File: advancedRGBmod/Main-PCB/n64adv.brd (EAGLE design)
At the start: 64.5 x 37.7 mm, 112 parts, among them U1 10CL010YE144, U2 ADV7125/ADV7123, U4 74LVC3G17, U5 S25FLXXXSO8-DUAL, U6 TLV70012DDC, U7 TLV70025DDC

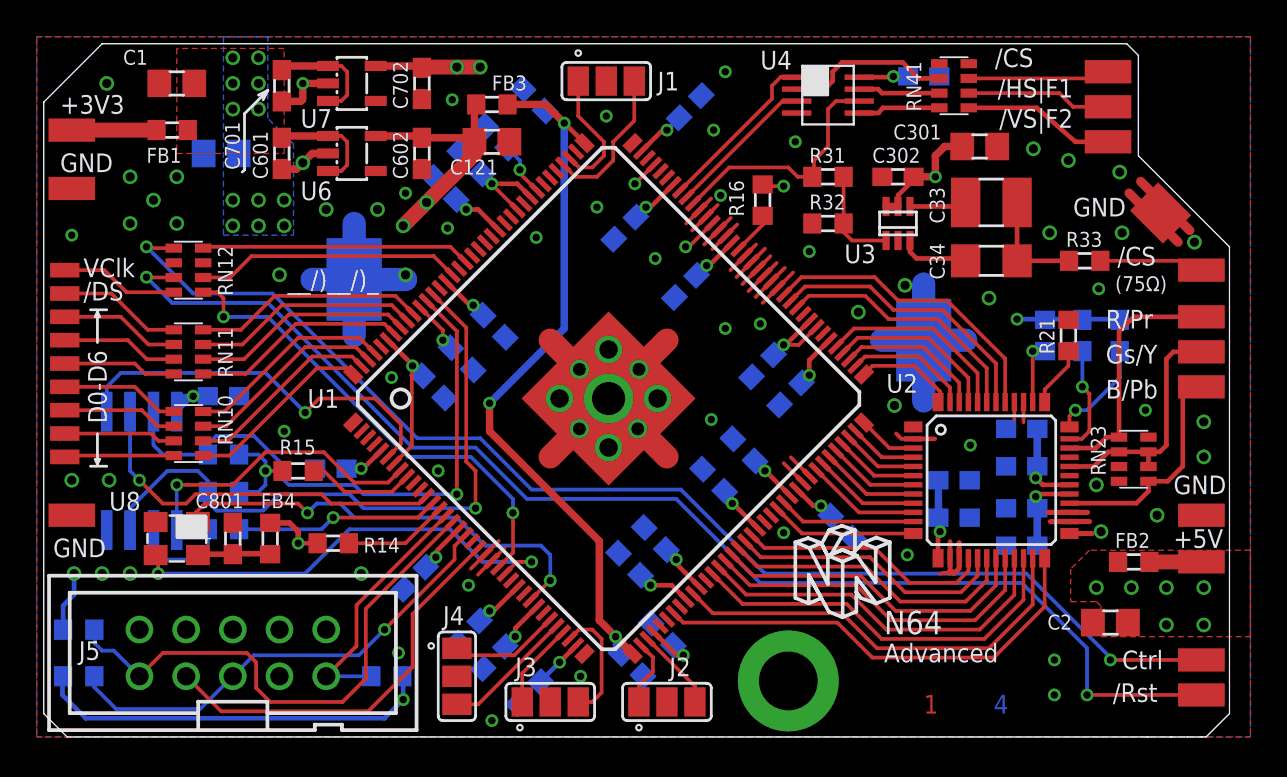
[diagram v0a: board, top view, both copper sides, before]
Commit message: pcb update: add some additional pads for rst and ctrl io
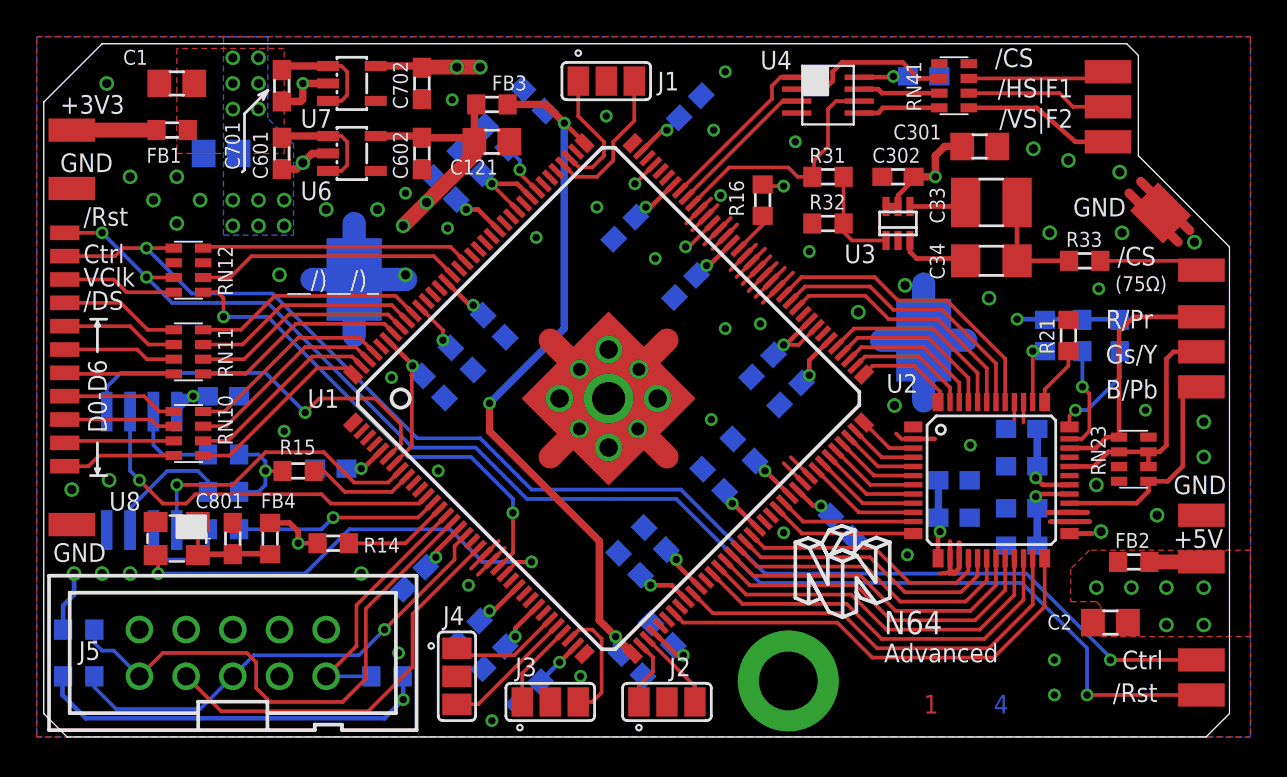
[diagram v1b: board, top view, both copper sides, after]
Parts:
- added /RST_A, CTRL_A: (no value), wirepad:SMD0,8-1,6
- moved D1 0.51 mm to (1.52, 16.0)
- moved D2 0.51 mm to (1.52, 17.3)
- moved D0 0.51 mm to (1.52, 14.7)
- moved CLOCK# 0.51 mm to (1.52, 24.9)
- moved D3 0.51 mm to (1.52, 18.5)
- moved D4 0.51 mm to (1.52, 19.8)
- moved D5 0.51 mm to (1.52, 21.1)
- moved D6 0.51 mm to (1.52, 22.4)
- moved DSYNC# 0.51 mm to (1.52, 23.6)
- moved P_GND1 0.51 mm to (1.91, 11.6)
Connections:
- removed net N$25: R52.1, U1.132, U5.3
- removed net N$74: R53.1, U1.133, U5.7
- removed net N$78: U1.28, U8.1
- new net N$56: R53.1, U5.7
- new net N$67: R52.1, U5.3
- net N$66: now also CTRL_A.P$1
- net N$70: now also /RST_A.P$1
- net VCCIO_CO: now also U8.1
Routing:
- net N$25: track 35.7 -> 0.00 mm, vias 1 -> 0
- net N$74: track 32.2 -> 0.00 mm, vias 1 -> 0
- net N$78: track 24.5 -> 0.00 mm, vias 2 -> 0
- net N$67: track 0.00 -> 7.09 mm
- net N$70: track 69.8 -> 75.2 mm, vias 2 -> 3
- net N$56: track 0.00 -> 5.00 mm
- net N$66: track 68.5 -> 73.1 mm
- net VCCIO_CO: track 4.16 -> 5.96 mm
- net GND: vias 73 -> 72
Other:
- outline, holes or cut-outs redrawn
- board text added: "N64A_20190109"
- board text added: "PCB Design (c) 2017-2019 Peter Bartmann"
- board text removed: "N64A_20181207"
- board text removed: "PCB Design (c) 2017-2018 Peter Bartmann"

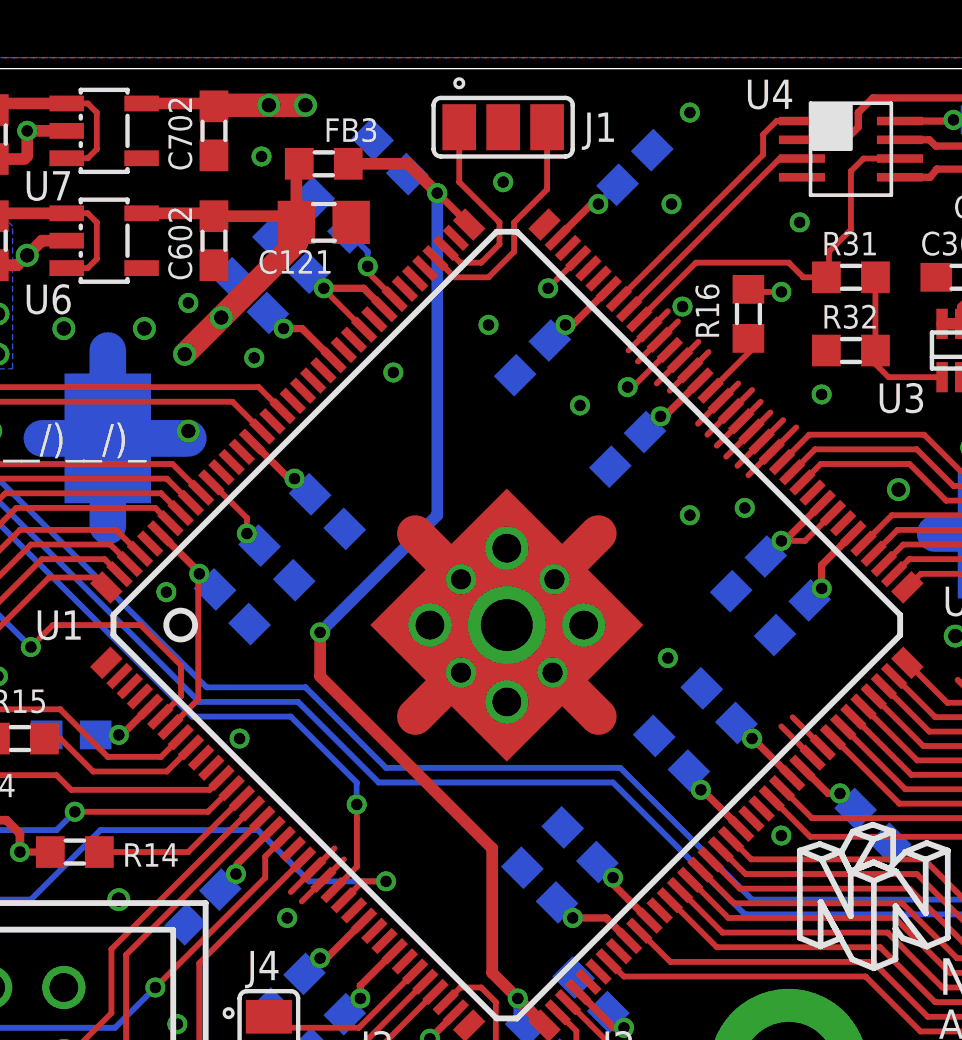
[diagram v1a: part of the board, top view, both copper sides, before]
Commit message: bank separation between digital video in and digital video outs using 2.5V LDO
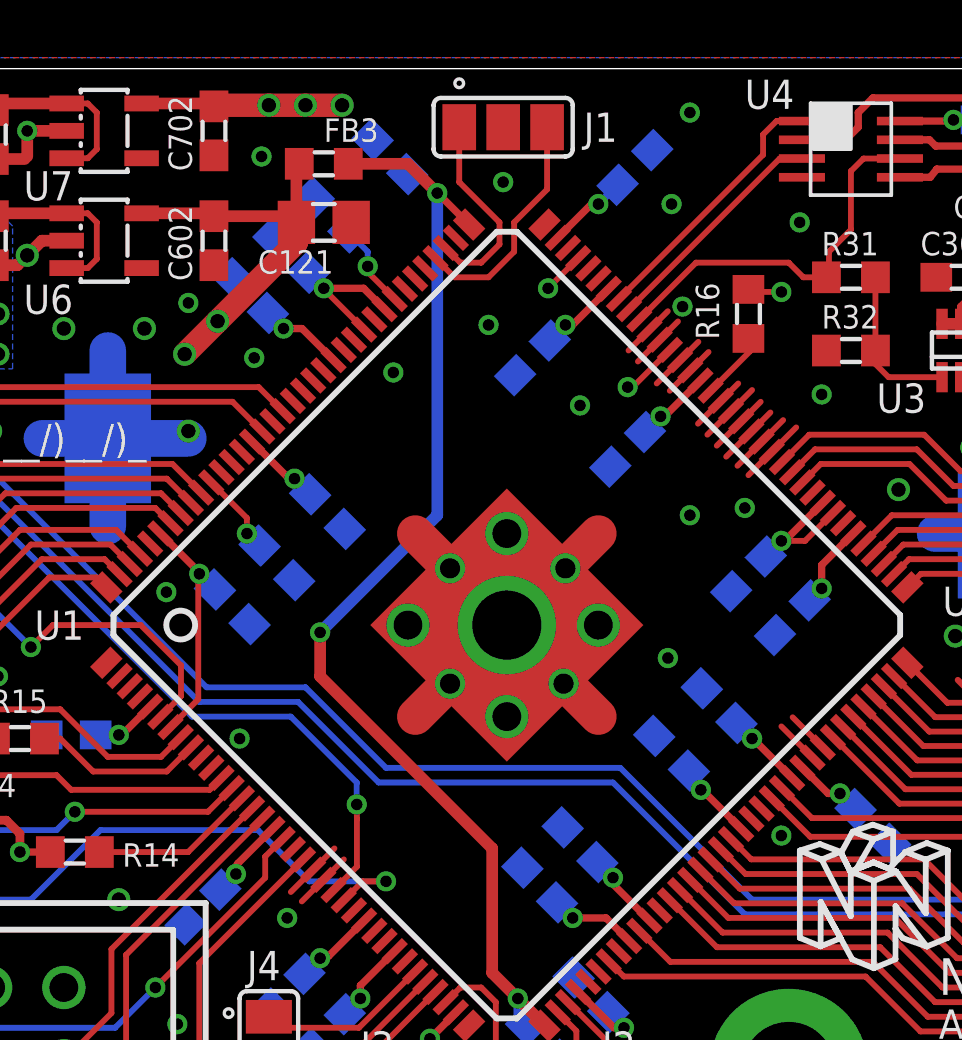
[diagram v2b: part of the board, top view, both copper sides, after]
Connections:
- net VCCA: now also C104.1, C105.1, C106.1, C107.1, C108.1, U1.40, U1.47, U1.56, U1.62, U1.80, U1.81
- net VCCIO: no longer C104.1, C105.1, C106.1, C107.1, C108.1, U1.40, U1.47, U1.56, U1.62, U1.80, U1.81
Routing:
- net VCCA: track 106.7 -> 123.7 mm, vias 6 -> 12
- net VCCIO: track 72.2 -> 56.4 mm, vias 29 -> 24
- added copper zone on layer 2, net DUMMY
- added copper zone on layer 15, net VCCA
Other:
- board text added: "N64A_20191005"
- board text removed: "N64A_20190109"

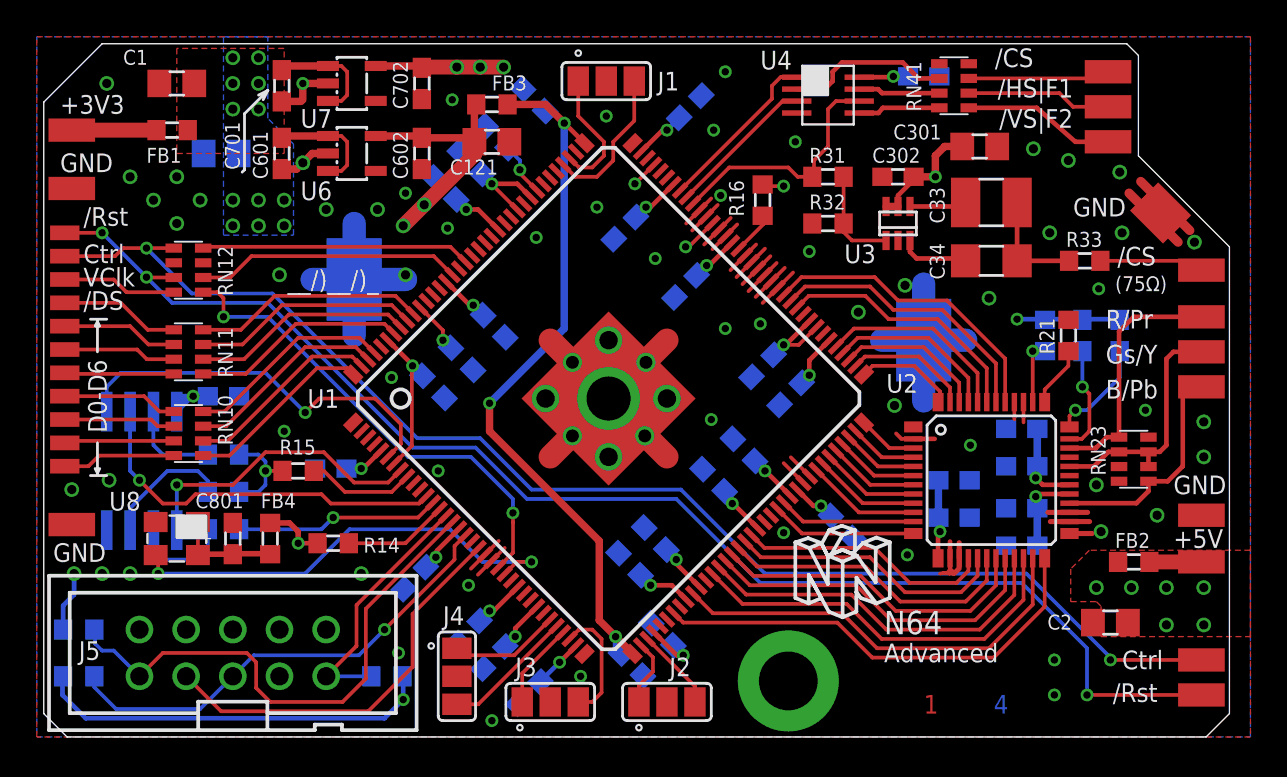
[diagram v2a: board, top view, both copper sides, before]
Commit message: update N64Adv board: - csync level selection by jumper - output IO bank powered by 5V rail (over a 3.3V ldo)
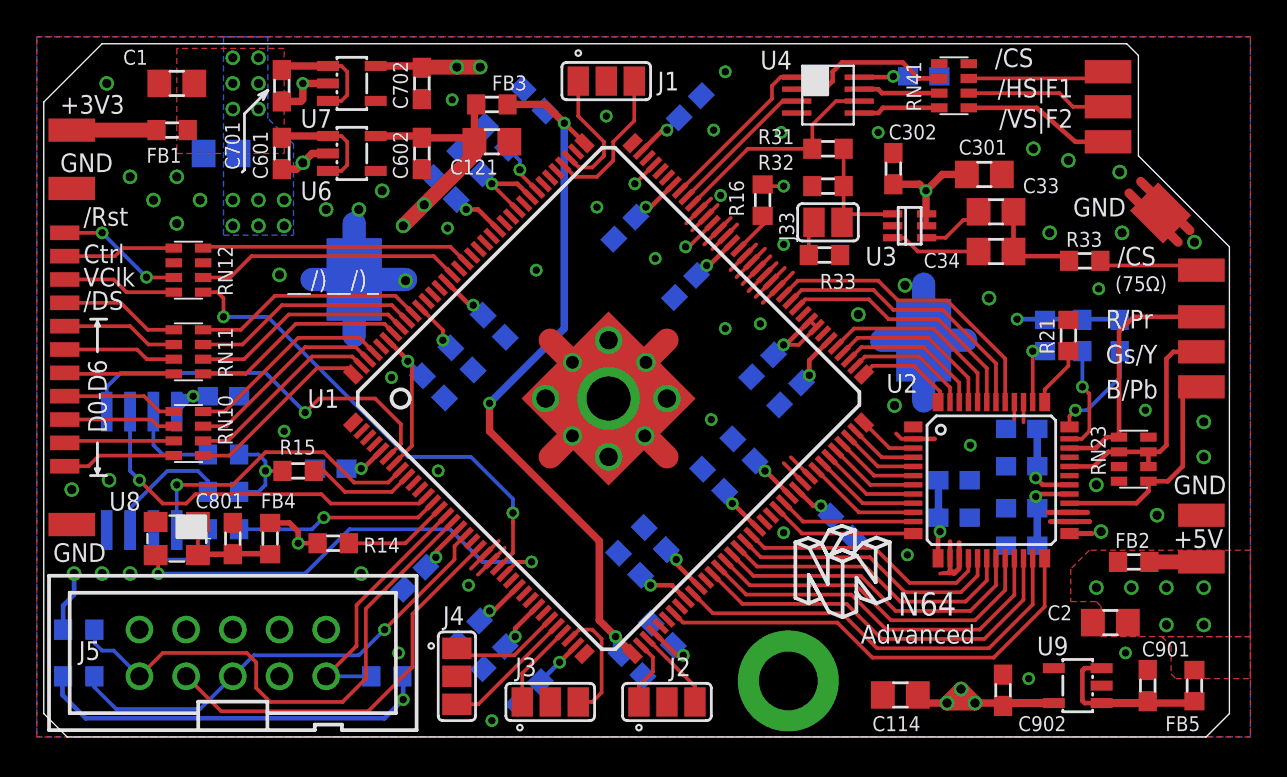
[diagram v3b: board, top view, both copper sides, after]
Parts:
- removed /RST_A, CTRL_A: (no value), wirepad:SMD0,8-1,6
- removed U$1: (no value), logo:ESD_10.00
- removed U$2: (no value), logo:MUELLTONNE_10.00
- added C114: 10u, rcl:C0805
- added C901, C902: 1u, rcl:C0603
- added FB5: MPZ1608S221A, rcl:R0603
- added J33: (no value), jumper:SJ
- added R34: 75, rcl:R0603
- added U9: TLV70033DDC, v-reg-micrel:SOT23-5
- /RST, CTRL: device wirepad@1:SMD1,27-2,54 -> wirepad:SMD0,8-1,6
- C33: device rcl@1:C1210 -> rcl:C0805
- C34: device rcl:C1206 -> rcl:C0805
- R32: value 475 -> 6k19
- R33: value 75 -> 523
- moved /RST 66.8 mm to (1.52, 27.4), turned to 270 degrees
- moved CTRL 65.6 mm to (1.52, 26.2), turned to 270 degrees
- moved R33 14.2 mm to (42.9, 26.2), turned to 180 degrees
- moved R32 2.03 mm to (43.1, 30.0)
- moved C301 1.55 mm to (51.6, 30.6)
- moved R31 1.52 mm to (43.1, 32.0)
- moved U3 0.65 mm to (47.5, 27.8), turned to 270 degrees
- moved C33 0.57 mm to (52.2, 28.6)
- moved C34 0.57 mm to (52.2, 26.4)
- moved C302 0.51 mm to (46.6, 30.9), turned to 90 degrees
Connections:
- new net A3V3: C104.1, C105.1, C106.1, C107.1, C108.1, C114.1, C902.1, U1.40, U1.47, U1.56, U1.62, U1.80, U1.81, U9.5
- new net N$25: C901.1, FB5.2, U9.1, U9.3
- new net N$71: J33.1, R33.2
- net +5V: now also FB5.1
- net GND: now also C114.2, C901.2, C902.2, R33.1, U9.2
- net N$1: now also J33.2
- net N$17: now also R34.1; no longer R33.1
- net N$21: now also R34.2; no longer R33.2
- net N$66: now also CTRL.P$1; no longer CTRL.1, CTRL_A.P$1
- net N$70: now also /RST.P$1; no longer /RST.1, /RST_A.P$1
- net VCCA: no longer C104.1, C105.1, C106.1, C107.1, C108.1, U1.40, U1.47, U1.56, U1.62, U1.80, U1.81
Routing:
- net N$70: track 75.2 -> 6.94 mm, vias 3 -> 2
- net N$66: track 73.1 -> 6.11 mm, vias 2 -> 0
- net A3V3: track 0.00 -> 34.1 mm, vias 0 -> 8
- net VCCA: track 123.7 -> 105.2 mm, vias 12 -> 6
- net N$25: track 0.00 -> 11.5 mm
- net N$71: track 0.00 -> 1.89 mm
- net N$16: track 3.85 -> 5.22 mm
- net CSYNC#: track 13.4 -> 12.1 mm
- net N$1: track 5.51 -> 6.82 mm
- net N$17: track 6.00 -> 5.40 mm
- added copper zone on layer 15, net A3V3
- removed copper zone on layer 15, net N$4
- removed copper zone on layer 2, net N$4
- removed copper zone on layer 15, net VCCA
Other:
- board text added: "N64A_20200305"
- board text added: "PCB Design (c) 2017-2020 Peter Bartmann"
- board text removed: "1"
- board text removed: "2"
- board text removed: "3"
- board text removed: "4"
- board text removed: "N64A_20191005"
- board text removed: "PCB Design (c) 2017-2019 Peter Bartmann"
